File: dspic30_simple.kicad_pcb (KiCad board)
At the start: 2 copper layers, 95.5 x 57 mm, 20 parts, among them J1 Jack-DC, J2 Conn_01x19_Pin, J4 Conn_01x21_Pin, SW1 SW_Push, U2 L7805

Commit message: revision rev D
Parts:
- removed D2: D, Diode_THT:D_DO-41_SOD81_P7.62mm_Horizontal
- removed R3: 100R, Resistor_THT:R_Axial_DIN0207_L6.3mm_D2.5mm_P7.62mm_Horizontal
- removed dsPIC30F4011: PIC18F4550-IP, Package_DIP:DIP-40_W15.24mm
- added C4: 22pF, Capacitor_THT:C_Disc_D7.0mm_W2.5mm_P5.00mm, F.Cu at (148.5, 94.5)
- added C8: 22pF, Capacitor_THT:C_Disc_D7.0mm_W2.5mm_P5.00mm, F.Cu at (143.5, 94.5)
- added JP1: Jumper_3_Bridged12, Connector_PinHeader_2.54mm:PinHeader_1x03_P2.54mm_Vertical, F.Cu at (108.5, 76.0)
- added JP2: Jumper_3_Bridged12, Connector_PinHeader_2.54mm:PinHeader_1x03_P2.54mm_Vertical, F.Cu at (109.0, 81.9)
- added U1: PIC18F4550-IP, Package_DIP:DIP-40_W15.24mm_Socket, F.Cu at (113.4, 86.2)
- added Y1: Crystal, Crystal:Resonator-2Pin_W8.0mm_H3.5mm, F.Cu at (149.0, 90.5)
- moved R1 14.8 mm to (103.5, 89.5), turned to -90 degrees
- moved SW1 4.32 mm to (114.0, 97.0)
- moved C1 3.04 mm to (97.5, 76.5)
- moved C6 0.90 mm to (139.0, 89.5)
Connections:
- C2 pad 1: /5VLDO -> /5VLDO_reg
- ICSP1 pad 1: /RESET -> /RESET_botton
- J2 pad 13: /CLKI -> unconnected-(J2-Pin_13-Pad13)
- J2 pad 14: /RC15 -> unconnected-(J2-Pin_14-Pad14)
- J4 pad 21: /5VLDO -> /5Vin
- R1 pad 2: /RESET_BOTON -> /RESET_Voltage
- SW1 pad 2: /RESET_BOTON -> /RESET_botton
- U2 pad 3: /5VLDO -> /5VLDO_reg
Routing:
- net /RESET_botton: track 0.00 -> 84.4 mm
- net /RESET: track 71.6 -> 0.00 mm
- net /RESET_BOTON: track 17.8 -> 0.00 mm
- net /5Vin: track 0.00 -> 15.8 mm
- net /CLKI: track 24.2 -> 9.07 mm
- net /5VLDO: track 177.2 -> 162.1 mm
- net /RESET_Voltage: track 0.00 -> 14.9 mm
- net /5VLDO_reg: track 0.00 -> 14.8 mm
- net /RC15: track 24.7 -> 10.1 mm
- net Net-(Dee1-K): track 22.3 -> 19.8 mm
- net GND: track 2.68 -> 3.35 mm

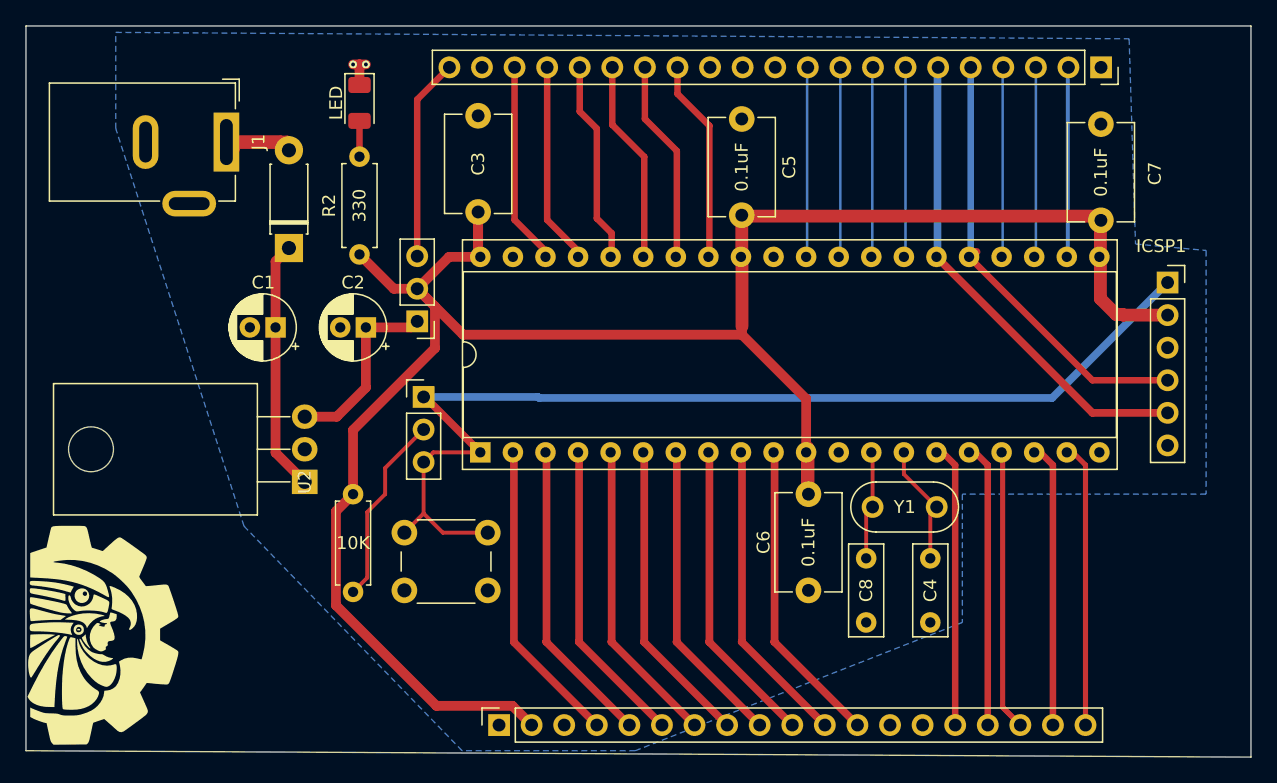
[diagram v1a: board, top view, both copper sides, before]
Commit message: feat(hw): bootstrap dsPIC33EP128MC206 dev‑kit (Rev A, pre‑rout)
• Añadido “sistema mínimo” (LDO 3 V3, reset RC, ICSP, filtrado) para DSPIC33EP128MC206‑I/PT
• Creado símbolo y asociado huella TQFP‑64 (0 .65 mm pitch)
• Colocación preliminar de MCU, conectores de alimentación, ICSP y headers PPS
• Asignadas/ajustadas huellas de todos los componentes (THT ↔ SMD)
• Proyecto listo para fase de enrutado y “ERC/DRC clean” inicial
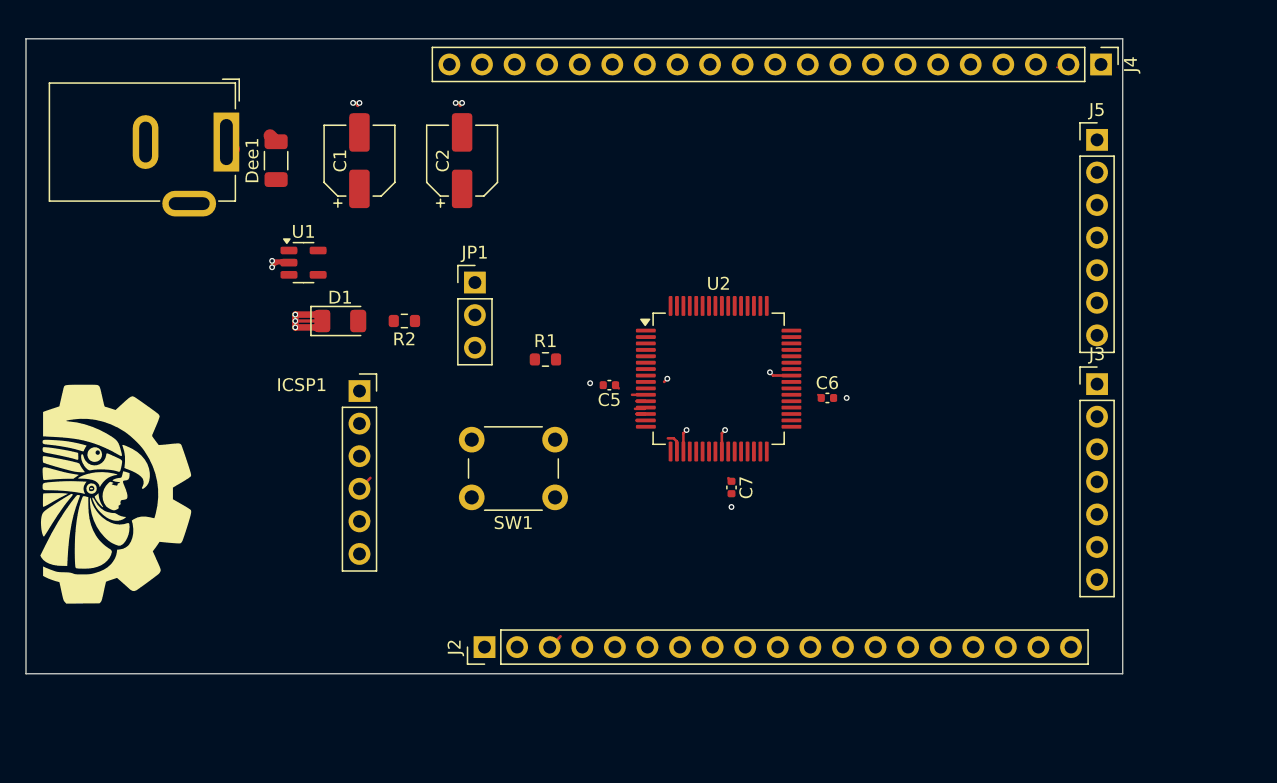
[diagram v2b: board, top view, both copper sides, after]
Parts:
- removed C3: 0.1uF, Capacitor_THT:C_Disc_D7.5mm_W5.0mm_P7.50mm
- removed C4, C8: 22pF, Capacitor_THT:C_Disc_D7.0mm_W2.5mm_P5.00mm
- removed JP2: Jumper_3_Bridged12, Connector_PinHeader_2.54mm:PinHeader_1x03_P2.54mm_Vertical
- removed Y1: Crystal, Crystal:Resonator-2Pin_W8.0mm_H3.5mm
- added J3: Conn_01x07_Pin, Connector_PinHeader_2.54mm:PinHeader_1x07_P2.54mm_Vertical, F.Cu at (161.5, 80.9)
- added J5: Conn_01x07_Pin, Connector_PinHeader_2.54mm:PinHeader_1x07_P2.54mm_Vertical, F.Cu at (161.5, 61.9)
- C1, C2: footprint Capacitor_THT:CP_Radial_D5.0mm_P2.00mm -> Capacitor_SMD:CP_Elec_5x3
- C5, C6, C7: footprint Capacitor_THT:C_Disc_D7.5mm_W5.0mm_P7.50mm -> Capacitor_SMD:C_0402_1005Metric
- Dee1: footprint Diode_THT:D_DO-41_SOD81_P7.62mm_Horizontal -> Capacitor_SMD:C_1206_3216Metric
- J2: footprint Connector_PinSocket_2.54mm:PinSocket_1x19_P2.54mm_Vertical -> Connector_PinHeader_2.54mm:PinHeader_1x19_P2.54mm_Vertical
- J4: footprint Connector_PinSocket_2.54mm:PinSocket_1x21_P2.54mm_Vertical -> Connector_PinHeader_2.54mm:PinHeader_1x21_P2.54mm_Vertical
- R1, R2: footprint Resistor_THT:R_Axial_DIN0207_L6.3mm_D2.5mm_P7.62mm_Horizontal -> Resistor_SMD:R_0603_1608Metric
- U1: value PIC18F4550-IP -> AP2127K-3.0; footprint Package_DIP:DIP-40_W15.24mm_Socket -> Package_TO_SOT_SMD:SOT-23-5
- U2: value L7805 -> DSPIC33EP128MC206-I/PT; footprint Package_TO_SOT_THT:TO-220-3_Horizontal_TabDown -> Package_QFP:LQFP-64_10x10mm_P0.5mm
- moved ICSP1 63.6 mm to (104.0, 81.5)
- moved C7 35.5 mm to (133.0, 89.0), turned to -90 degrees
- moved U2 33.3 mm to (132.0, 80.5), turned to 0 degrees
- moved U1 20.2 mm to (99.6, 71.5), turned to 0 degrees
- moved R1 18.3 mm to (118.5, 79.0), turned to 0 degrees
- moved D1 17.1 mm to (102.5, 76.0), turned to 0 degrees
- moved C5 16.8 mm to (123.5, 81.0), turned to 180 degrees
- moved C2 15.0 mm to (112.0, 63.5), turned to 90 degrees
- moved C1 14.6 mm to (104.0, 63.5), turned to 90 degrees
- moved G*** 11.0 mm to (87.5, 89.5)
- moved SW1 8.95 mm to (119.2, 89.8)
- moved C6 7.64 mm to (140.5, 82.0), turned to 0 degrees
- moved Dee1 6.88 mm to (97.5, 63.5)
- moved R2 6.26 mm to (107.5, 76.0), turned to 180 degrees
- moved J2 6.18 mm to (113.8, 101.4)
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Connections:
- ICSP1 pad 1: /RESET_botton -> /*MCLR
- J2 pad 10: /RB6 -> /PGD
- J2 pad 11: /RB7 -> /RC0
- J2 pad 12: /RB8 -> /RC1
- J2 pad 13: unconnected-(J2-Pin_13-Pad13) -> /RC2
- J2 pad 14: unconnected-(J2-Pin_14-Pad14) -> /RC11
- J2 pad 15: /RC13 -> /RE12
- J2 pad 16: /RC14 -> /RE13
- J2 pad 17: /RE8 -> /RE14
- J2 pad 18: /RD1 -> /RE15
- J2 pad 19: /RD3 -> /RA8
- J2 pad 2: /5VLDO -> unconnected-(J2-Pin_2-Pad2)
- J2 pad 3: GND -> /RA12
- J2 pad 4: /RBO -> /RA11
- J2 pad 5: /RB1 -> /RA0
- J2 pad 6: /RB2 -> /RA1
- J2 pad 7: /RB3 -> /RB0
- J2 pad 8: /RB4 -> /RB1
- J2 pad 9: /RB5 -> /PGC
- J4 pad 1: unconnected-(J4-Pin_1-Pad1) -> /RB9
- J4 pad 10: /RF0 -> /RB13
- J4 pad 11: GND -> /RB12
- J4 pad 12: GND -> /RB11
- J4 pad 13: GND -> /RB10
- J4 pad 14: /RE5 -> /RF1
- J4 pad 15: /RE4 -> /RF0
- J4 pad 16: /RE3 -> /RA7
- J4 pad 17: /RE2 -> /RB14
- J4 pad 18: /RE1 -> /RB15
- J4 pad 19: /RE0 -> /RG6
- J4 pad 2: /RD2 -> /RC6
- J4 pad 20: GND -> /RG7
- J4 pad 21: /5Vin -> /RG8
- J4 pad 3: /RD0 -> /RC7
- J4 pad 4: /RF6 -> /RC8
- J4 pad 5: /PGD -> /RD5
- J4 pad 6: /PGC -> /RD6
- J4 pad 7: /RF5 -> /RC9
- J4 pad 8: /RF4 -> /RD7
- J4 pad 9: /RF1 -> /RA10
- R1 pad 2: /RESET_Voltage -> /*MCLR
- SW1 pad 2: /RESET_botton -> /*MCLR
- U1 pad 1: /RESET_botton -> Net-(Dee1-K)
- U1 pad 2: /RBO -> GND
- U1 pad 3: /RB1 -> unconnected-(U1-EN-Pad3)
- U1 pad 4: /RB2 -> unconnected-(U1-NC-Pad4)
- U1 pad 5: /RB3 -> /5VLDO_reg
- U2 pad 1: Net-(Dee1-K) -> /RA7
- U2 pad 2: GND -> /RB14
- U2 pad 3: /5VLDO_reg -> /RB15
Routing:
- net /5VLDO: track 162.1 -> 1.06 mm
- net /RESET_botton: track 84.4 -> 0.00 mm
- net /PGC: track 37.5 -> 0.00 mm
- net /PGD: track 34.4 -> 2.80 mm
- net /RB7: track 24.3 -> 0.00 mm
- net /RB6: track 24.3 -> 0.00 mm
- net /RB4: track 24.3 -> 0.00 mm
- net /RB2: track 24.3 -> 0.00 mm
- net /RB8: track 24.3 -> 0.00 mm
- net /RB5: track 24.3 -> 0.00 mm
- net /RB3: track 24.3 -> 0.00 mm
- net /RBO: track 24.3 -> 0.00 mm
- net /RB1: track 24.3 -> 0.13 mm
- net /RE8: track 24.2 -> 0.00 mm
- net /RD1: track 24.2 -> 0.00 mm
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- removed copper zone on B.Cu, net GND
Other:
- board size 95.5 x 57 mm -> 85.5 x 49.5 mm
